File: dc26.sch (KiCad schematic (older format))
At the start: 60 parts, among them J1 CONN_01X10, J2 CONN_01X10, J3 CONN_01X10

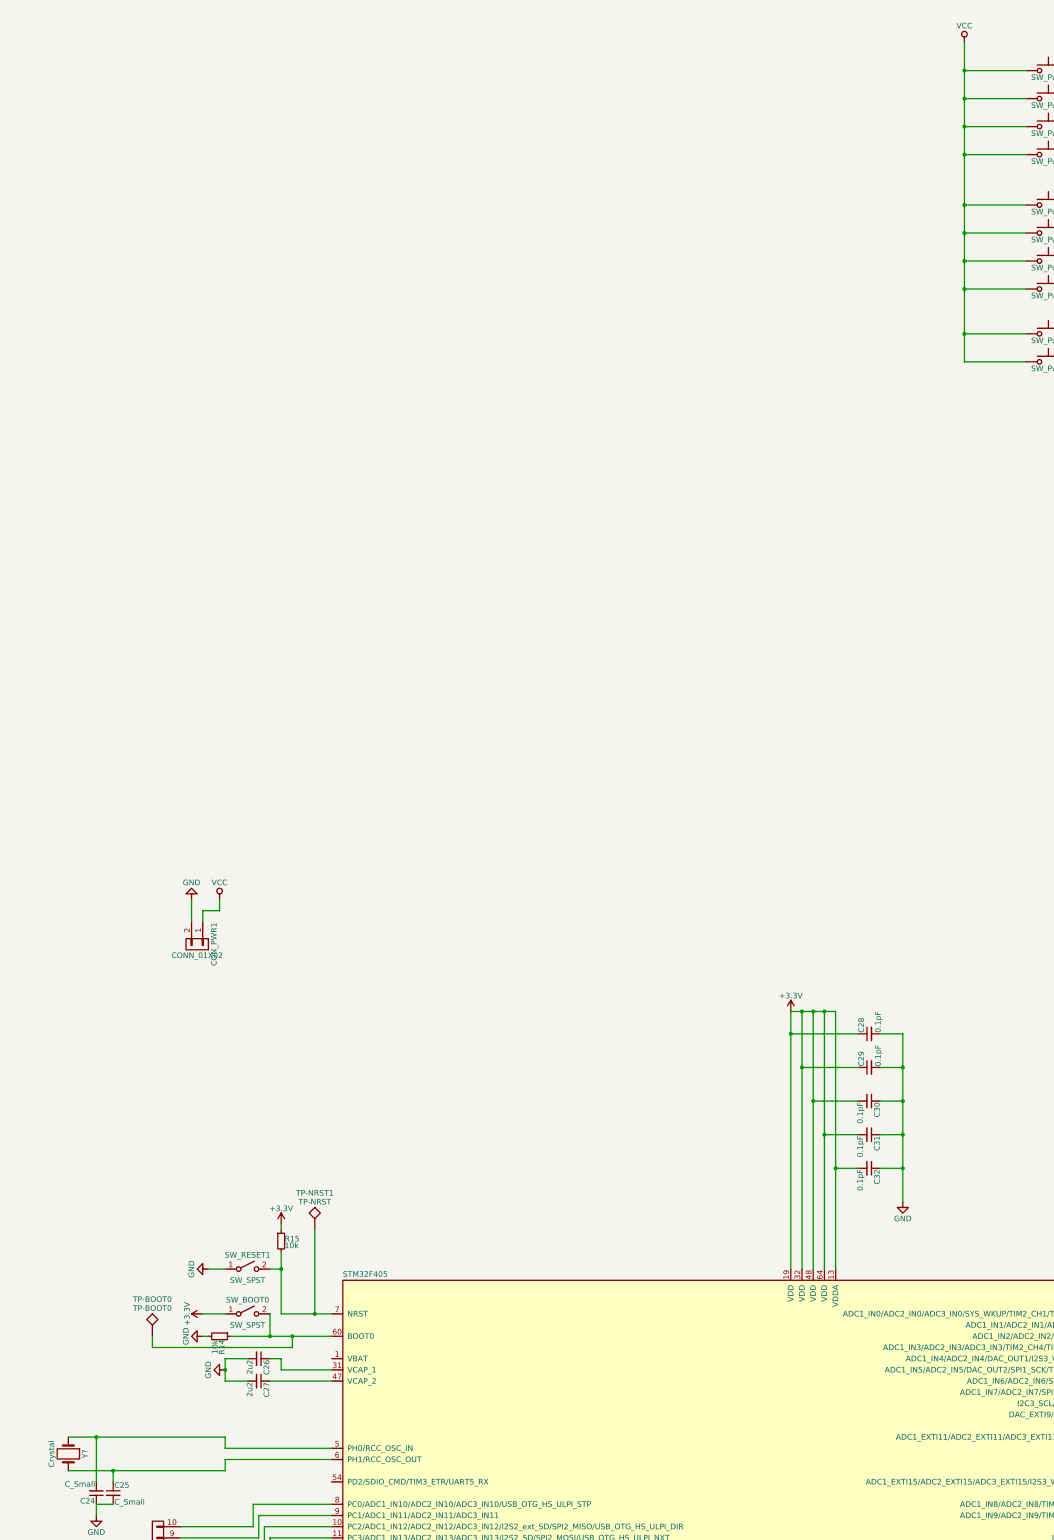
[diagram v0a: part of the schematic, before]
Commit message: splitting led power out from 5v so that we can insert the mosfet
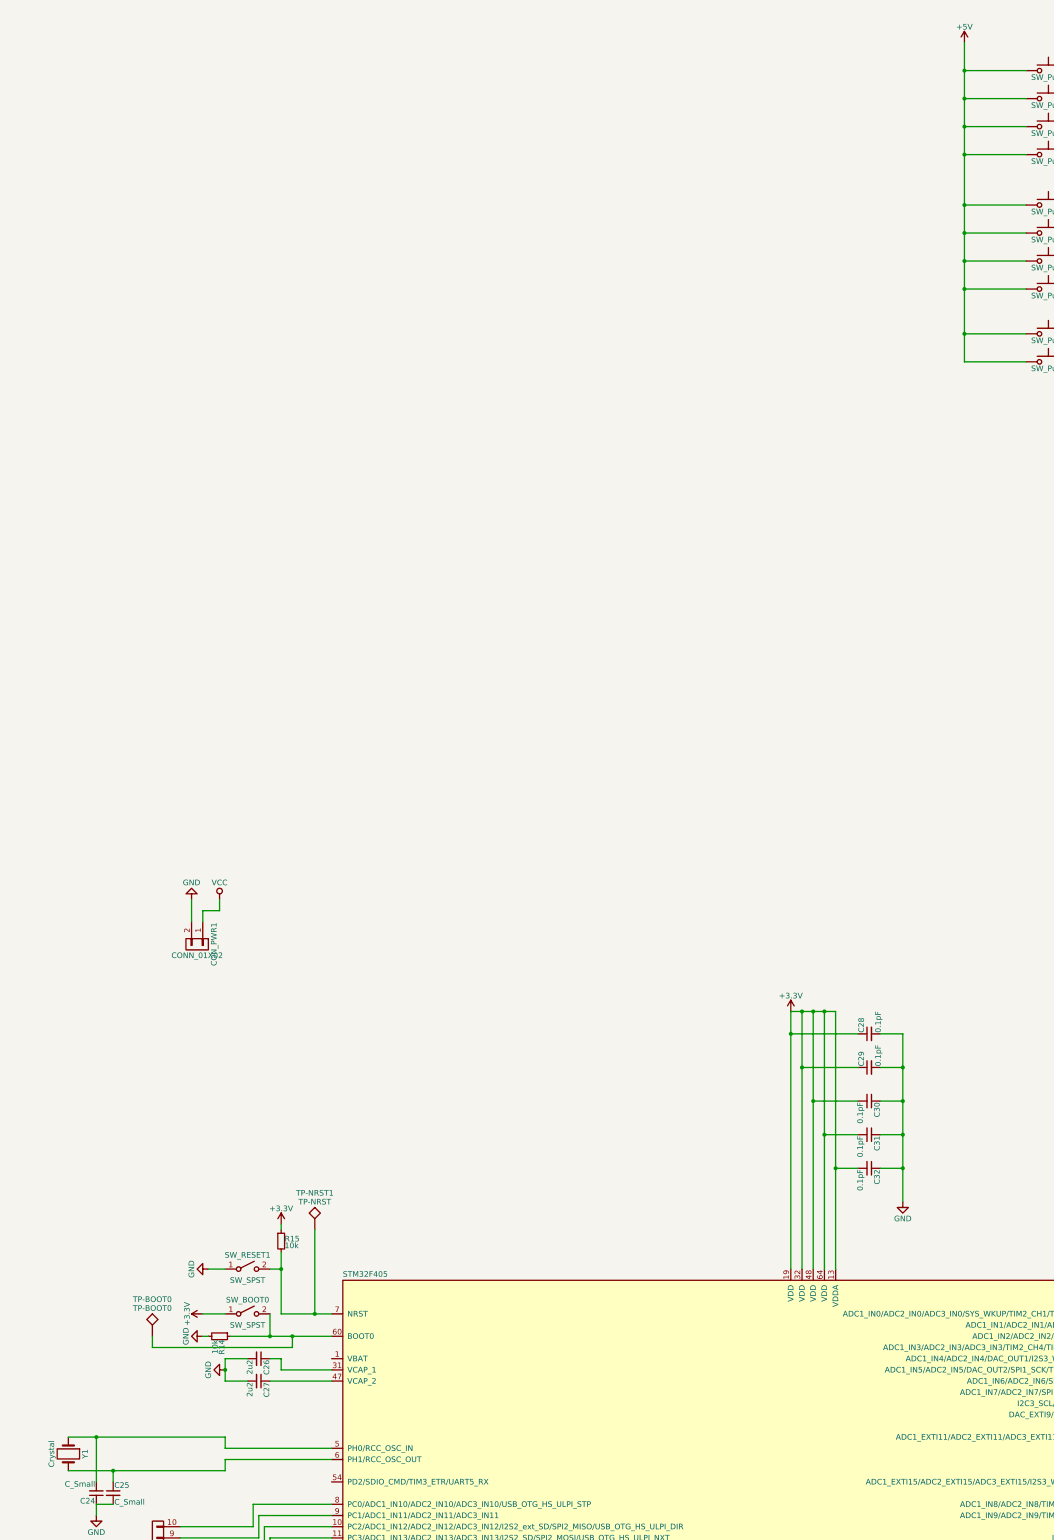
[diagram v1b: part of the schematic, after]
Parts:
- gave numbers to parts that had none: 1
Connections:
- net VCC: no longer B_L1.1, B_L2.1, B_L3.1, B_L4.1, B_R1.1, B_R2.1, B_R3.1, B_R4.1, B_SELECT1.1, B_START1.1
- new net +5V: B_L1.1, B_L2.1, B_L3.1, B_L4.1, B_R1.1, B_R2.1, B_R3.1, B_R4.1, B_SELECT1.1, B_START1.1
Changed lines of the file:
@@
 $EndComp
 $Comp
-L VCC #PWR01
-U 1 1 5AD008FD
-P -5650 -6600
-F 0 "#PWR01" H -5650 -6750 50  0001 C CNN
-F 1 "VCC" H -5650 -6450 50  0000 C CNN
-F 2 "" H -5650 -6600 50  0001 C CNN
-F 3 "" H -5650 -6600 50  0001 C CNN
-	1    -5650 -6600
-	1    0    0    -1
-$EndComp
-$Comp
-L GND #PWR02
+L GND #PWR18
 U 1 1 5AD27FBE
 P -3800 -6700
-F 0 "#PWR02" H -3800 -6950 50  0001 C CNN
+F 0 "#PWR18" H -3800 -6950 50  0001 C CNN
 F 1 "GND" H -3800 -6850 50  0000 C CNN
 F 2 "" H -3800 -6700 50  0001 C CNN
@@
 $EndComp
 $Comp
-L GND #PWR03
+L GND #PWR2
 U 1 1 5AD5BD83
 P -12550 1050
-F 0 "#PWR03" H -12550 800 50  0001 C CNN
+F 0 "#PWR2" H -12550 800 50  0001 C CNN
 F 1 "GND" H -12550 900 50  0000 C CNN
 F 2 "" H -12550 1050 50  0001 C CNN
@@
 $EndComp
 $Comp
-L VCC #PWR04
+L VCC #PWR6
 U 1 1 5AD5C4E4
 P -12300 1050
-F 0 "#PWR04" H -12300 900 50  0001 C CNN
+F 0 "#PWR6" H -12300 900 50  0001 C CNN
 F 1 "VCC" H -12300 1200 50  0000 C CNN
 F 2 "" H -12300 1050 50  0001 C CNN
@@
 $EndComp
 $Comp
-L GND #PWR05
+L GND #PWR20
 U 1 1 5AD6E593
 P -2500 -5100
-F 0 "#PWR05" H -2500 -5350 50  0001 C CNN
+F 0 "#PWR20" H -2500 -5350 50  0001 C CNN
 F 1 "GND" H -2500 -5250 50  0000 C CNN
 F 2 "" H -2500 -5100 50  0001 C CNN
@@
 $EndComp
 $Comp
-L GND #PWR06
+L GND #PWR21
 U 1 1 5AD6F999
 P -2500 -3550
-F 0 "#PWR06" H -2500 -3800 50  0001 C CNN
+F 0 "#PWR21" H -2500 -3800 50  0001 C CNN
 F 1 "GND" H -2500 -3700 50  0000 C CNN
 F 2 "" H -2500 -3550 50  0001 C CNN
@@
 $EndComp
 $Comp
-L GND #PWR07
+L GND #PWR19
 U 1 1 5AD77A72
 P -3600 -800
-F 0 "#PWR07" H -3600 -1050 50  0001 C CNN
+F 0 "#PWR19" H -3600 -1050 50  0001 C CNN
 F 1 "GND" H -3600 -950 50  0000 C CNN
 F 2 "" H -3600 -800 50  0001 C CNN
@@
 $EndComp
 $Comp
-L VCC #PWR08
+L VCC #PWR11
 U 1 1 5AD946E2
 P -7100 12550
-F 0 "#PWR08" H -7100 12400 50  0001 C CNN
+F 0 "#PWR11" H -7100 12400 50  0001 C CNN
 F 1 "VCC" H -7100 12700 50  0000 C CNN
 F 2 "" H -7100 12550 50  0001 C CNN
@@
 $EndComp
 $Comp
-L GND #PWR09
+L GND #PWR10
 U 1 1 5AD98D43
 P -7100 12200
-F 0 "#PWR09" H -7100 11950 50  0001 C CNN
+F 0 "#PWR10" H -7100 11950 50  0001 C CNN
 F 1 "GND" H -7100 12050 50  0000 C CNN
 F 2 "" H -7100 12200 50  0001 C CNN
@@
 $EndComp
 $Comp
-L GND #PWR010
+L GND #PWR17
 U 1 1 5ADAF5CF
 P -3950 10600
-F 0 "#PWR010" H -3950 10350 50  0001 C CNN
+F 0 "#PWR17" H -3950 10350 50  0001 C CNN
 F 1 "GND" H -3950 10450 50  0000 C CNN
 F 2 "" H -3950 10600 50  0001 C CNN
@@
 $EndComp
 $Comp
-L GND #PWR011
+L GND #PWR15
 U 1 1 5ADAFD4C
 P -4000 9500
-F 0 "#PWR011" H -4000 9250 50  0001 C CNN
+F 0 "#PWR15" H -4000 9250 50  0001 C CNN
 F 1 "GND" H -4000 9350 50  0000 C CNN
 F 2 "" H -4000 9500 50  0001 C CNN
@@
 $EndComp
 $Comp
-L GND #PWR012
+L GND #PWR16
 U 1 1 5ADB04C2
 P -4000 12400
-F 0 "#PWR012" H -4000 12150 50  0001 C CNN
+F 0 "#PWR16" H -4000 12150 50  0001 C CNN
 F 1 "GND" H -4000 12250 50  0000 C CNN
 F 2 "" H -4000 12400 50  0001 C CNN
@@
 $EndComp
 $Comp
-L GND #PWR013
+L GND #PWR12
 U 1 1 5B04F2A2
 P -7000 8800
-F 0 "#PWR013" H -7000 8550 50  0001 C CNN
+F 0 "#PWR12" H -7000 8550 50  0001 C CNN
 F 1 "GND" H -7000 8650 50  0000 C CNN
 F 2 "" H -7000 8800 50  0001 C CNN
@@
 $EndComp
 $Comp
-L GND #PWR014
+L GND #PWR1
 U 1 1 5B0E23AB
 P -13400 6550
-F 0 "#PWR014" H -13400 6300 50  0001 C CNN
+F 0 "#PWR1" H -13400 6300 50  0001 C CNN
 F 1 "GND" H -13400 6400 50  0000 C CNN
 F 2 "" H -13400 6550 50  0001 C CNN
@@
 $EndComp
 $Comp
-L +3.3V #PWR016
+L +3.3V #PWR9
 U 1 1 5B0D3E01
 P -7200 2050
-F 0 "#PWR016" H -7200 1900 50  0001 C CNN
+F 0 "#PWR9" H -7200 1900 50  0001 C CNN
 F 1 "+3.3V" H -7200 2190 50  0000 C CNN
 F 2 "" H -7200 2050 50  0001 C CNN
@@
 $EndComp
 $Comp
-L GND #PWR017
+L GND #PWR7
 U 1 1 5B0F137D
 P -12250 5250
-F 0 "#PWR017" H -12250 5000 50  0001 C CNN
+F 0 "#PWR7" H -12250 5000 50  0001 C CNN
 F 1 "GND" H -12250 5100 50  0000 C CNN
 F 2 "" H -12250 5250 50  0001 C CNN
@@
 $EndComp
 $Comp
-L GND #PWR018
+L GND #PWR13
 U 1 1 5B0F6A9C
 P -6200 3750
-F 0 "#PWR018" H -6200 3500 50  0001 C CNN
+F 0 "#PWR13" H -6200 3500 50  0001 C CNN
 F 1 "GND" H -6200 3600 50  0000 C CNN
 F 2 "" H -6200 3750 50  0001 C CNN
@@
 $EndComp
 $Comp
-L +3.3V #PWR019
+L +3.3V #PWR8
 U 1 1 5B11C638
 P -11750 3950
-F 0 "#PWR019" H -11750 3800 50  0001 C CNN
+F 0 "#PWR8" H -11750 3800 50  0001 C CNN
 F 1 "+3.3V" H -11750 4090 50  0000 C CNN
 F 2 "" H -11750 3950 50  0001 C CNN
@@
 $EndComp
 $Comp
-L GND #PWR020
+L GND #PWR5
 U 1 1 5B12677B
 P -12400 4350
-F 0 "#PWR020" H -12400 4100 50  0001 C CNN
+F 0 "#PWR5" H -12400 4100 50  0001 C CNN
 F 1 "GND" H -12400 4200 50  0000 C CNN
 F 2 "" H -12400 4350 50  0001 C CNN
@@
 $EndComp
 $Comp
-L GND #PWR021
+L GND #PWR4
 U 1 1 5B1309D3
 P -12450 4950
-F 0 "#PWR021" H -12450 4700 50  0001 C CNN
+F 0 "#PWR4" H -12450 4700 50  0001 C CNN
 F 1 "GND" H -12450 4800 50  0000 C CNN
 F 2 "" H -12450 4950 50  0001 C CNN
@@
 $EndComp
 $Comp
-L +3.3V #PWR022
+L +3.3V #PWR3
 U 1 1 5B136E3C
 P -12450 4750
-F 0 "#PWR022" H -12450 4600 50  0001 C CNN
+F 0 "#PWR3" H -12450 4600 50  0001 C CNN
 F 1 "+3.3V" H -12450 4890 50  0000 C CNN
 F 2 "" H -12450 4750 50  0001 C CNN
@@
 $EndComp
 $Comp
-L GND #PWR023
+L GND #PWR22
 U 1 1 5B13B631
 P -1800 6650
-F 0 "#PWR023" H -1800 6400 50  0001 C CNN
+F 0 "#PWR22" H -1800 6400 50  0001 C CNN
 F 1 "GND" H -1800 6500 50  0000 C CNN
 F 2 "" H -1800 6650 50  0001 C CNN
@@
 $EndComp
 $Comp
-L GND #PWR024
+L GND #PWR23
 U 1 1 5B1B7467
 P -1200 9050
-F 0 "#PWR024" H -1200 8800 50  0001 C CNN
+F 0 "#PWR23" H -1200 8800 50  0001 C CNN
 F 1 "GND" H -1200 8900 50  0000 C CNN
 F 2 "" H -1200 9050 50  0001 C CNN
@@
 	-13400 6450 -13400 6550
 $Comp
-L Crystal Y?
+L Crystal Y1
 U 1 1 5B113127
 P -13650 6000
-F 0 "Y?" H -13650 6150 50  0000 C CNN
+F 0 "Y1" H -13650 6150 50  0000 C CNN
 F 1 "Crystal" H -13650 5850 50  0000 C CNN
 F 2 "Crystals:Crystal_SMD_5032-2pin_5.0x3.2mm" H -13650 6000 50  0001 C CNN
@@
 	-13250 6250 -13250 6150
 Connection ~ -13250 6150
+$Comp
+L +5V #PWR?
+U 1 1 5B123F56
+P -5650 -6600
+F 0 "#PWR?" H -5650 -6750 50  0001 C CNN
+F 1 "+5V" H -5650 -6460 50  0000 C CNN
+F 2 "" H -5650 -6600 50  0001 C CNN
+F 3 "" H -5650 -6600 50  0001 C CNN
+	1    -5650 -6600
+	1    0    0    -1
+$EndComp
 $EndSCHEMATC

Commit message: Footprint updates
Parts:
- C24, C25: value C_Small -> 22pF
- C26, C27: footprint Capacitors_SMD:C_0603 -> Capacitors_SMD:C_0805
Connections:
- net LED-POWER-ENABLE: now reaches STM32F405.50 (ADC1_EXTI15/ADC2_EXTI15/ADC3_EXTI15/I2S3_WS/SPI1_NSS/SPI3_NSS/SYS_JTDI/TIM2_CH1/TIM2_ETR/PA15)
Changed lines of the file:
@@
 P -13250 6350
 F 0 "C25" H -13240 6420 50  0000 L CNN
-F 1 "C_Small" H -13240 6270 50  0000 L CNN
+F 1 "22pF" H -13240 6270 50  0000 L CNN
 F 2 "Capacitors_SMD:C_0603" H -13250 6350 50  0001 C CNN
 F 3 "" H -13250 6350 50  0001 C CNN
@@
 P -13400 6350
 F 0 "C24" H -13390 6420 50  0000 L CNN
-F 1 "C_Small" H -13390 6270 50  0000 L CNN
+F 1 "22pF" H -13390 6270 50  0000 L CNN
 F 2 "Capacitors_SMD:C_0603" H -13400 6350 50  0001 C CNN
 F 3 "" H -13400 6350 50  0001 C CNN
@@
 F 0 "C27" H -11940 5420 50  0000 L CNN
 F 1 "2u2" H -11940 5270 50  0000 L CNN
-F 2 "Capacitors_SMD:C_0603" H -11950 5350 50  0001 C CNN
+F 2 "Capacitors_SMD:C_0805" H -11950 5350 50  0001 C CNN
 F 3 "" H -11950 5350 50  0001 C CNN
 	1    -11950 5350
@@
 F 0 "C26" H -11940 5220 50  0000 L CNN
 F 1 "2u2" H -11940 5070 50  0000 L CNN
-F 2 "Capacitors_SMD:C_0603" H -11950 5150 50  0001 C CNN
+F 2 "Capacitors_SMD:C_0805" H -11950 5150 50  0001 C CNN
 F 3 "" H -11950 5150 50  0001 C CNN
 	1    -11950 5150
@@
 Connection ~ -13250 6150
 $Comp
-L +5V #PWR?
+L +5V #PWR14
 U 1 1 5B123F56
 P -5650 -6600
-F 0 "#PWR?" H -5650 -6750 50  0001 C CNN
+F 0 "#PWR14" H -5650 -6750 50  0001 C CNN
 F 1 "+5V" H -5650 -6460 50  0000 C CNN
 F 2 "" H -5650 -6600 50  0001 C CNN
@@
 	1    0    0    -1
 $EndComp
+Text GLabel -1550 6250 2    60   Input ~ 0
+LED-POWER-ENABLE
+Wire Wire Line
+	-2700 6250 -1550 6250
 $EndSCHEMATC

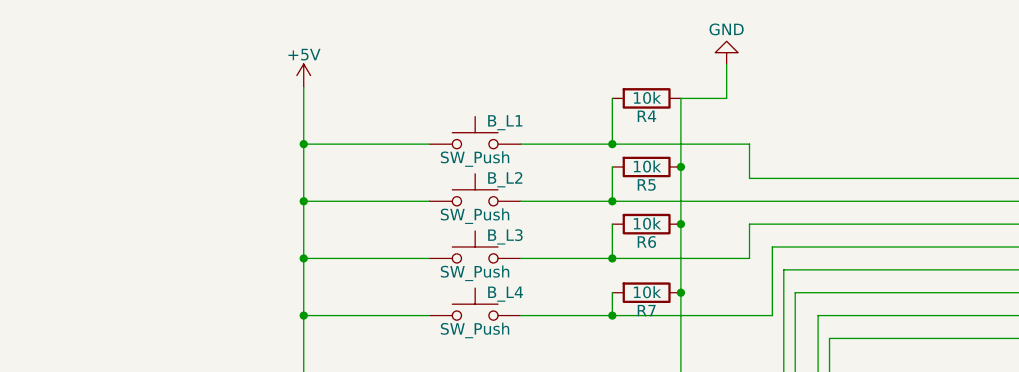
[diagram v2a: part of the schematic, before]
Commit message: Futher cleanup and footprint work, as well as power circuit fixes
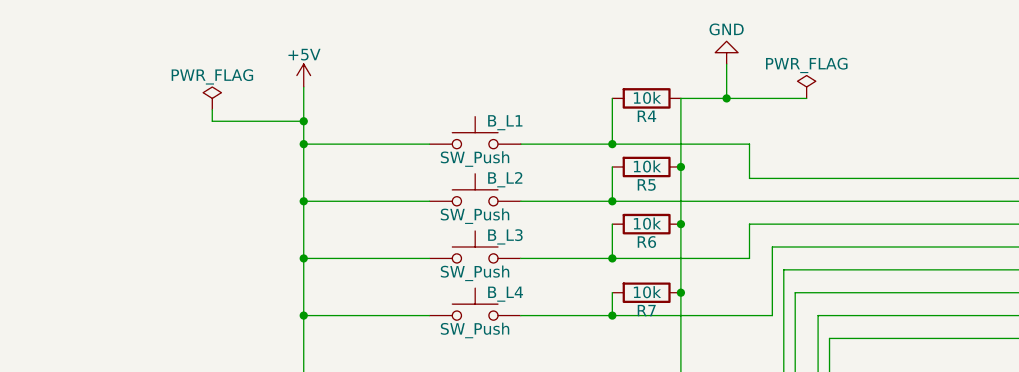
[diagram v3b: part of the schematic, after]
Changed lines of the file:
@@
 	-3800 -6700 -3800 -6550
 Wire Wire Line
-	-3800 -6550 -4000 -6550
+	-4000 -6550 -3450 -6550
 Wire Wire Line
 	-4000 -6550 -4000 -3900
@@
 Wire Wire Line
 	-2700 6250 -1550 6250
+$Comp
+L PWR_FLAG #FLG?
+U 1 1 5B18689B
+P -6050 -6500
+F 0 "#FLG?" H -6050 -6425 50  0001 C CNN
+F 1 "PWR_FLAG" H -6050 -6350 50  0000 C CNN
+F 2 "" H -6050 -6500 50  0001 C CNN
+F 3 "" H -6050 -6500 50  0001 C CNN
+	1    -6050 -6500
+	1    0    0    -1
+$EndComp
+Wire Wire Line
+	-6050 -6450 -5650 -6450
+Connection ~ -5650 -6450
+Wire Wire Line
+	-6050 -6450 -6050 -6500
+$Comp
+L PWR_FLAG #FLG?
+U 1 1 5B18707E
+P -3450 -6550
+F 0 "#FLG?" H -3450 -6475 50  0001 C CNN
+F 1 "PWR_FLAG" H -3450 -6400 50  0000 C CNN
+F 2 "" H -3450 -6550 50  0001 C CNN
+F 3 "" H -3450 -6550 50  0001 C CNN
+	1    -3450 -6550
+	1    0    0    -1
+$EndComp
+Connection ~ -3800 -6550
 $EndSCHEMATC
